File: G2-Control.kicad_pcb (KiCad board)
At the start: 2 copper layers, 100 x 100 mm, 93 parts, among them J1 Conn_01x06_Pin, J102 Conn_01x06_Pin, J103 Conn_01x06_Pin, J104 Board Interconnect, J2 Q2_link, J3 Conn_01x07_Pin, J4 Conn_01x05_Pin, K1 AZ822-2C-24DSE, K2 AZ822-2C-24DSE, K3 AZ822-2C-24DSE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

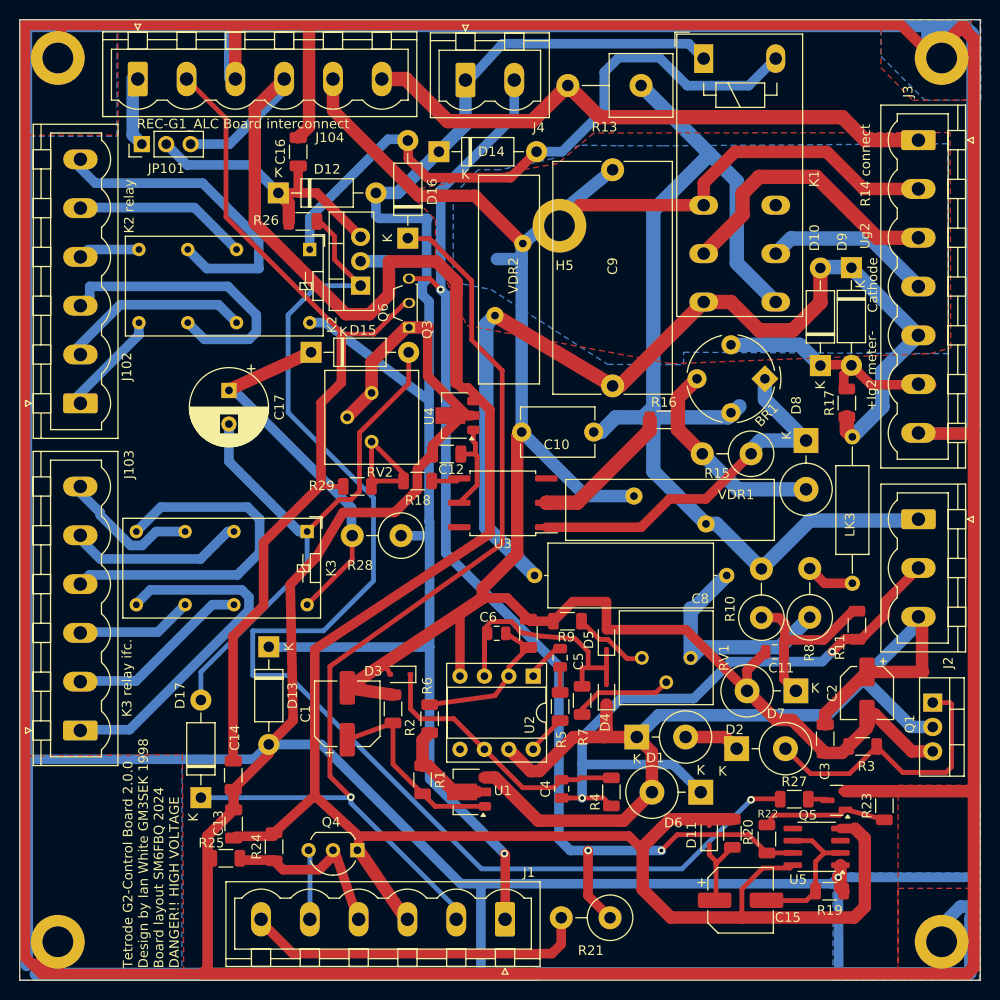
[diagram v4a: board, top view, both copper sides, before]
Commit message: Updated format to KiCad 9. Included footprints etc.
Standardized PCB layers, updated property formatting, and adjusted net assignments. Added some DigiKey, Electrokit, and Mouser component part numbers.
Reduced font sizes for better readability and incorporated embedded font settings.
Removed the sequencer from the schematic which wasn't really meant to be there.
Revised and excluded drc and erc warnings and exclusions.
Included footprints into the project library that formerly was defined outside of the project.
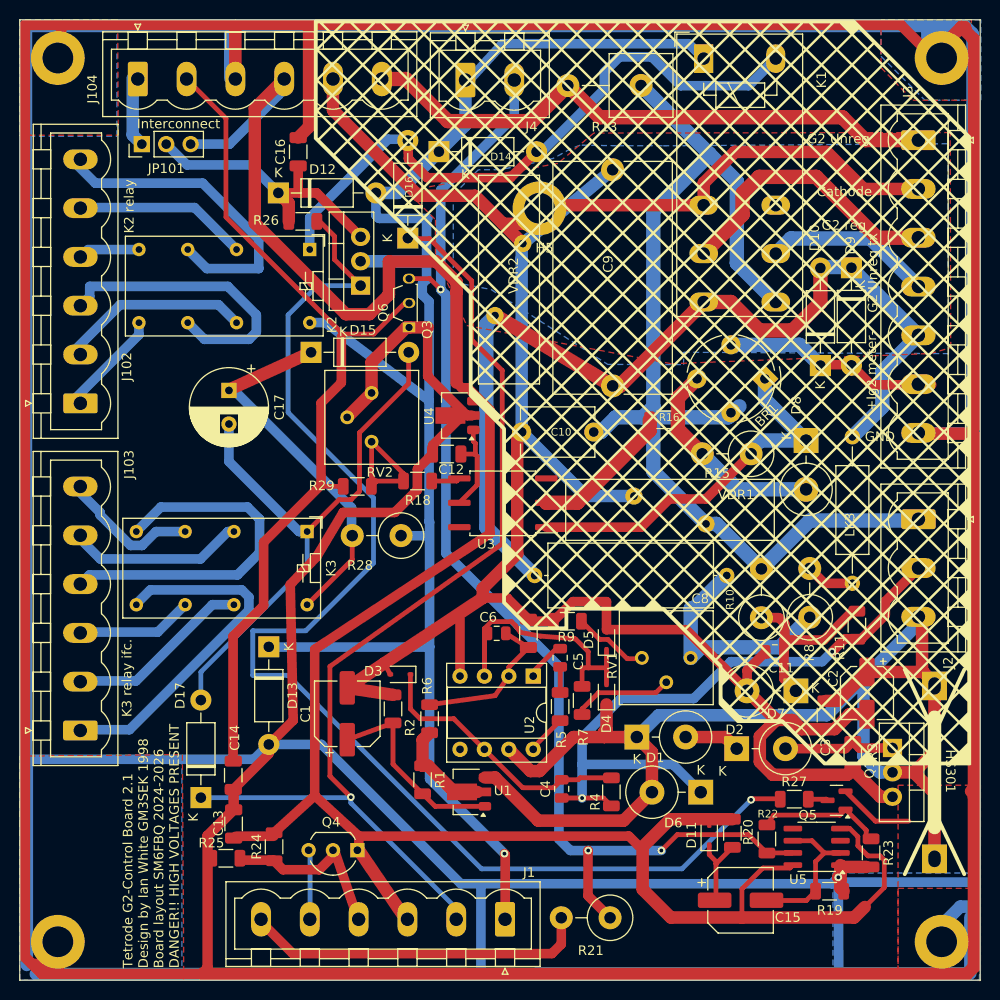
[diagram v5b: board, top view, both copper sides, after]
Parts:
- removed R17: Meter shunt, Resistor_SMD:R_1206_3216Metric
- added HS301: Heatsink_Pad_2Pin, Project_library:6025DG_Cooler, F.Cu at (175.3, 118.4)
- J104: value Board Interconnect -> Board Interconnect
- K1: value AZ822-2C-24DSE -> Schrack RTE24024
- Q3: footprint Package_TO_SOT_THT:TO-92S_Wide -> Project_library:TO-92S_Wide
- R19: value 1M -> 330k*
- R20: value 100k* -> 100k
- R28: value 820 1W* -> 680 1W*
- U3: footprint Package_SO:SOP-6_6.62x6.62mm_P2.54mm -> Project_library:SOP-6_6.62x6.62mm_P2.54mm
- moved Q1 6.31 mm to (170.9, 115.8)
- moved R23 5.10 mm to (168.7, 126.7), turned to -90 degrees
- moved H5 2.77 mm to (134.1, 59.6)
- moved C3 2.47 mm to (164.0, 112.4)
- moved R3 1.38 mm to (166.8, 116.6), turned to 90 degrees
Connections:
- net /Aux trip renamed /AUX_TRIP_L
- net GNDPWR renamed GND
- net Net-(J102-Pin_1) renamed /K2C_NO
- net Net-(J102-Pin_2) renamed /K2C_com
- net Net-(J102-Pin_3) renamed /K2C_NC
- net Net-(J102-Pin_4) renamed /K2B_NO
- net Net-(J102-Pin_5) renamed /K2B_com
- net Net-(J102-Pin_6) renamed /K2B_NC
- net Net-(J103-Pin_1) renamed /K3C_NO
- net Net-(J103-Pin_2) renamed /K3C_com
- net Net-(J103-Pin_3) renamed /K3C_NC
- net Net-(J103-Pin_4) renamed /K3B_NO
- net Net-(J103-Pin_5) renamed /K3B_com
- net Net-(J103-Pin_6) renamed /K3B_NC
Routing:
- net /+30V rail: track 110.1 -> 135.0 mm
- net Net-(D2-A): track 29.4 -> 11.8 mm
- net /CATHODE: track 234.8 -> 247.5 mm
- net /+Ig2: track 25.9 -> 22.8 mm
- net /-Ig2: track 103.6 -> 101.3 mm
- net +12V: track 239.9 -> 242.0 mm
- net GND: track 1027.9 -> 1026.6 mm
- net Net-(D14-A): track 67.7 -> 66.5 mm
- net Net-(Q6-G): track 134.2 -> 133.1 mm
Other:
- board text added: "+12V"
- board text added: "G2 Reg"
- board text added: "G2 Unreg Tx"
- board text added: "G2 Unreg tx"
- board text added: "G2 reg"
- board text added: "Interconnect"
- board text added: "K"
- board text added: "Tetrode G2-Control Board 2.1 Design by Ian White GM3SEK 1998 Board layout SM6FBQ 2024-2026 DANGER!! HIGH VOLTAGES PRESENT"
- board text removed: "+12V Reg"
- board text removed: "G2 Reg out"
- board text removed: "G2 Unreg In"
- board text removed: "G2 Unreg TX"
- board text removed: "R14 connect"
- board text removed: "REC-G1_ALC Board interconnect"
- board text removed: "Tetrode G2-Control Board 2.0.0 Design by Ian White GM3SEK 1998 Board layout SM6FBQ 2024 DANGER!! HIGH VOLTAGE"
- board text removed: "Ug2"
